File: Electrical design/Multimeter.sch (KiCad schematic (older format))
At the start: 36 parts, among them P101 CONN_02X07, P102 CONN_01X06, Q101 Q_PMOS_GSD, Q102 Q_NMOS_GSD, U101 STM32F373R8Tx, U102 ILI9341_LCD_Breakout, U103 BD4835, Y101 8 MHz

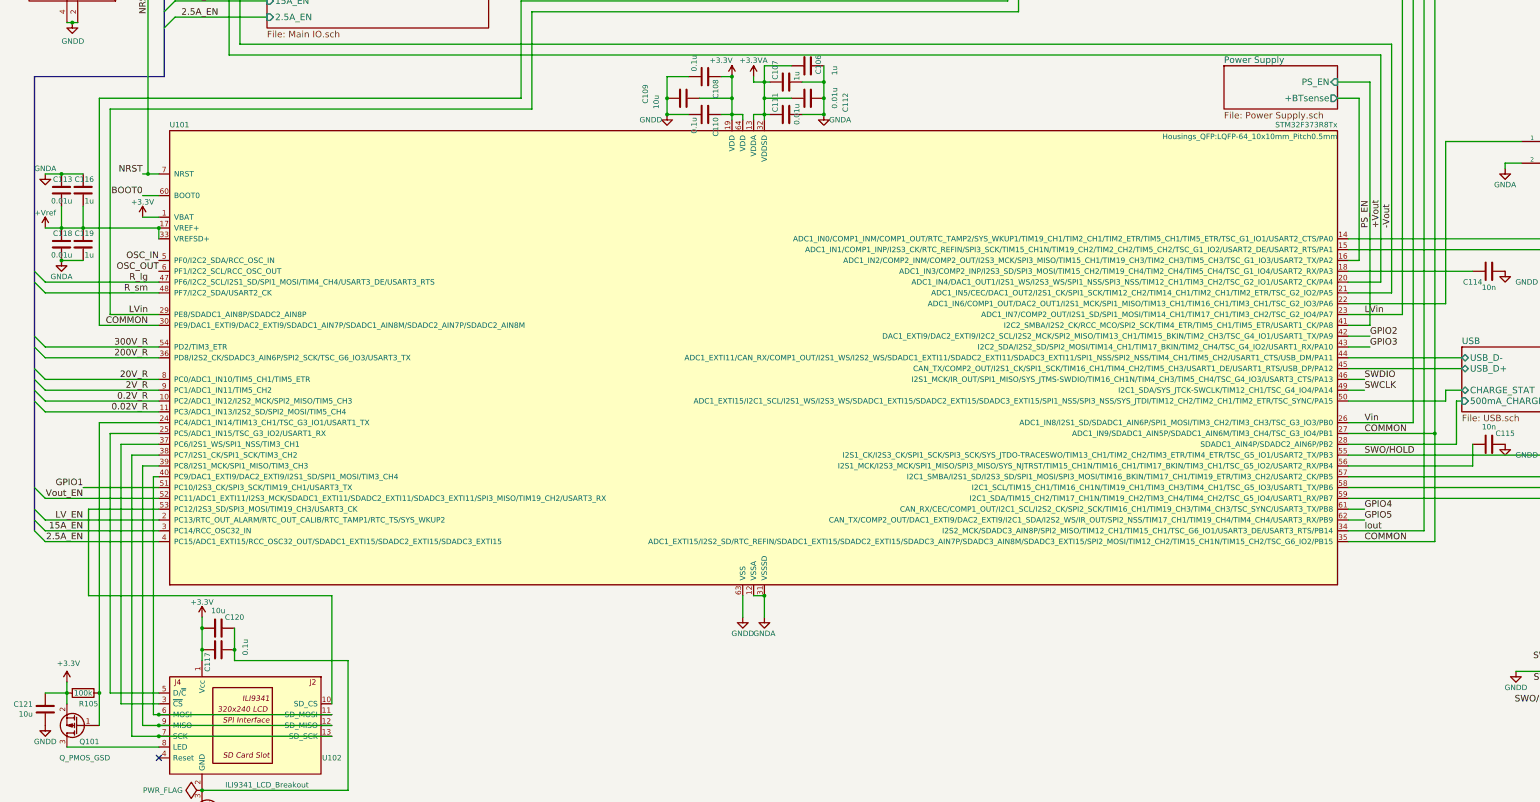
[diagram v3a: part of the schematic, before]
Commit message: Added PCB layout.
Also minor changes to schematic, the most major being changes
to which MCU pins control what to make the PCB layout easier.
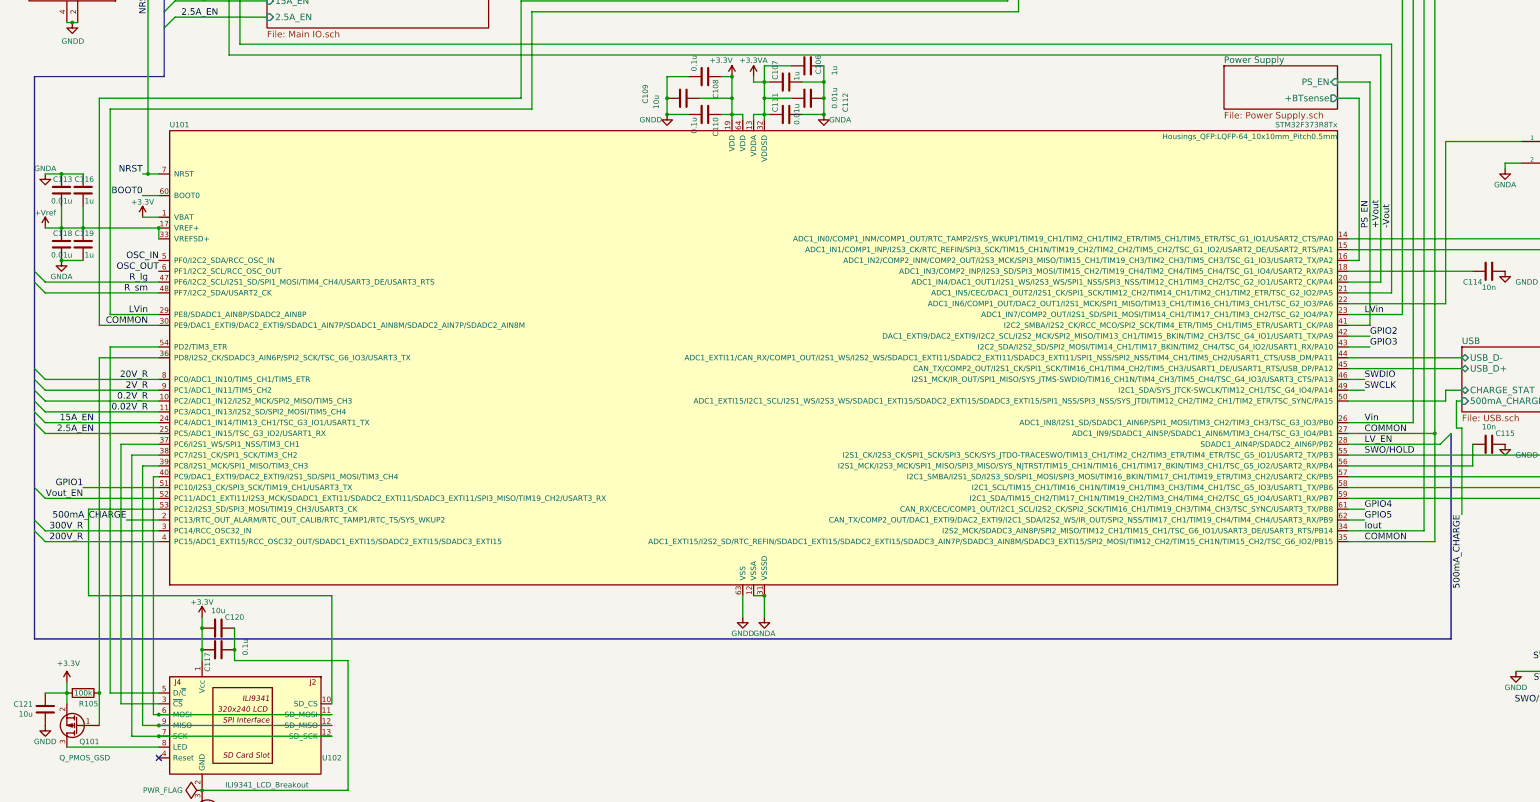
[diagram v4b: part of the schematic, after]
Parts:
- JP101: footprint Pin_Headers:Pin_Header_Straight_1x02 -> my footprints:Pin_Header_Straight_1x02
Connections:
- net USB/500mA_CHARGE is gone; now on net LV_EN: U101.28 (SDADC1_AIN4P/SDADC2_AIN6P/PB2)
- net 15A_EN: now also U101.24 (PC4/ADC1_IN14/TIM13_CH1/TSC_G3_IO1/USART1_TX); no longer U101.3 (PC14/RCC_OSC32_IN)
- net 2.5A_EN: now also U101.25 (PC5/ADC1_IN15/TSC_G3_IO2/USART1_RX); no longer U101.4 (PC15/ADC1_EXTI15/RCC_OSC32_OUT/SDADC1_EXTI15/SDADC2_EXTI15/SDADC3_EXTI15)
- net 200V_R: now also U101.4 (PC15/ADC1_EXTI15/RCC_OSC32_OUT/SDADC1_EXTI15/SDADC2_EXTI15/SDADC3_EXTI15); no longer U101.36 (PD8/I2S2_CK/SDADC3_AIN6P/SPI2_SCK/TSC_G6_IO3/USART3_TX)
- net 300V_R: now also U101.3 (PC14/RCC_OSC32_IN); no longer U101.54 (PD2/TIM3_ETR)
- net LV_EN: no longer U101.2 (PC13/RTC_OUT_ALARM/RTC_OUT_CALIB/RTC_TAMP1/RTC_TS/SYS_WKUP2)
- net at Q101.1 (G), R105.1: now also U101.36 (PD8/I2S2_CK/SDADC3_AIN6P/SPI2_SCK/TSC_G6_IO3/USART3_TX); no longer U101.24 (PC4/ADC1_IN14/TIM13_CH1/TSC_G3_IO1/USART1_TX)
- net at U102.5 (D/~C): now also U101.54 (PD2/TIM3_ETR); no longer U101.25 (PC5/ADC1_IN15/TSC_G3_IO2/USART1_RX)
- new net 500mA_CHARGE: U101.2 (PC13/RTC_OUT_ALARM/RTC_OUT_CALIB/RTC_TAMP1/RTC_TS/SYS_WKUP2)
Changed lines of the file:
@@
 Sheet 1 5
 Title "Multimeter – Overview"
-Date "2016-06-22"
-Rev "0.5"
+Date "2016-07-02"
+Rev "0.6"
 Comp ""
-Comment1 ""
+Comment1 "Licensed under the GNU GPL v3"
 Comment2 ""
 Comment3 ""
@@
 F 0 "JP101" V 1450 1898 50  0000 L CNN
 F 1 "BOOT0" H 1460 1790 50  0001 C CNN
-F 2 "Pin_Headers:Pin_Header_Straight_1x02" H 1450 1850 50  0001 C CNN
+F 2 "my footprints:Pin_Header_Straight_1x02" H 1450 1850 50  0001 C CNN
 F 3 "" H 1450 1850 50  0000 C CNN
 	1    1450 1850
@@
 	700  5900 800  6000
 Entry Wire Line
-	700  6400 800  6500
-Entry Wire Line
-	700  6500 800  6600
+	700  7100 800  7200
+Entry Wire Line
+	700  7200 800  7300
 Entry Wire Line
 	700  6700 800  6800
@@
 	700  7800 800  7900
 Entry Wire Line
-	700  8000 800  8100
-Entry Wire Line
 	700  8100 800  8200
-Text Label 1150 8300 2    60   ~ 0
+Text Label 1250 7300 2    60   ~ 0
 2.5A_EN
-Text Label 1150 8200 2    60   ~ 0
+Text Label 1250 7200 2    60   ~ 0
 15A_EN
-Text Label 1150 8100 2    60   ~ 0
+Text Label 13000 7400 0    60   ~ 0
 LV_EN
 Text Label 1750 5900 2    60   ~ 0
@@
 Entry Wire Line
 	700  7000 800  7100
-Text Label 1750 6500 2    60   ~ 0
+Text Label 1150 8200 2    60   ~ 0
 300V_R
-Text Label 1750 6600 2    60   ~ 0
+Text Label 1150 8300 2    60   ~ 0
 200V_R
 Text Label 1750 6800 2    60   ~ 0
@@
 PS_EN
 $Comp
-L +3.3V #PWR019
+L +3.3V #PWR018
 U 1 1 574F1A1A
 P 1000 9600
-F 0 "#PWR019" H 1000 9450 50  0001 C CNN
+F 0 "#PWR018" H 1000 9450 50  0001 C CNN
 F 1 "+3.3V" H 1015 9773 50  0000 C CNN
 F 2 "" H 1000 9600 50  0000 C CNN
@@
 $EndComp
 $Comp
-L GNDD #PWR020
+L GNDD #PWR019
 U 1 1 574F2BEE
 P 800 10000
-F 0 "#PWR020" H 800 9750 50  0001 C CNN
+F 0 "#PWR019" H 800 9750 50  0001 C CNN
 F 1 "GNDD" H 800 9850 50  0000 C CNN
 F 2 "" H 800 10000 50  0000 C CNN
@@
 $EndComp
 $Comp
-L GNDD #PWR021
+L GNDD #PWR020
 U 1 1 575818F5
 P 14300 7400
-F 0 "#PWR021" H 14300 7150 50  0001 C CNN
+F 0 "#PWR020" H 14300 7150 50  0001 C CNN
 F 1 "GNDD" H 14500 7300 50  0000 C CNN
 F 2 "" H 14300 7400 50  0000 C CNN
@@
 GPIO5
 $Comp
-L +3.3V #PWR022
+L +3.3V #PWR021
 U 1 1 5758136C
 P 7100 2300
-F 0 "#PWR022" H 7100 2150 50  0001 C CNN
+F 0 "#PWR021" H 7100 2150 50  0001 C CNN
 F 1 "+3.3V" H 7115 2473 50  0000 C CNN
 F 2 "" H 7100 2300 50  0000 C CNN
@@
 $EndComp
 $Comp
-L +3.3VA #PWR023
+L +3.3VA #PWR022
 U 1 1 5758157D
 P 6200 2300
-F 0 "#PWR023" H 6200 2150 50  0001 C CNN
+F 0 "#PWR022" H 6200 2150 50  0001 C CNN
 F 1 "+3.3VA" H 6215 2473 50  0000 C CNN
 F 2 "" H 6200 2300 50  0000 C CNN
@@
 $EndComp
 $Comp
-L +Vref #PWR024
+L +Vref #PWR023
 U 1 1 57581671
 P 6000 2400
-F 0 "#PWR024" H 6000 2250 50  0001 C CNN
+F 0 "#PWR023" H 6000 2250 50  0001 C CNN
 F 1 "+Vref" H 6015 2573 50  0000 C CNN
 F 2 "" H 6000 2400 50  0000 C CNN
@@
 $EndComp
 $Comp
-L GNDA #PWR025
+L GNDA #PWR024
 U 1 1 57581765
 P 6200 2900
-F 0 "#PWR025" H 6200 2650 50  0001 C CNN
+F 0 "#PWR024" H 6200 2650 50  0001 C CNN
 F 1 "GNDA" H 6205 2727 50  0000 C CNN
 F 2 "" H 6200 2900 50  0000 C CNN
@@
 $EndComp
 $Comp
-L GNDD #PWR026
+L GNDD #PWR025
 U 1 1 57581859
 P 7100 2900
-F 0 "#PWR026" H 7100 2650 50  0001 C CNN
+F 0 "#PWR025" H 7100 2650 50  0001 C CNN
 F 1 "GNDD" H 7105 2727 50  0000 C CNN
 F 2 "" H 7100 2900 50  0000 C CNN
@@
 $EndComp
 $Comp
-L GNDA #PWR027
+L GNDA #PWR026
 U 1 1 575E7712
 P 14300 4850
-F 0 "#PWR027" H 14300 4600 50  0001 C CNN
+F 0 "#PWR026" H 14300 4600 50  0001 C CNN
 F 1 "GNDA" H 14300 4700 50  0000 C CNN
 F 2 "" H 14300 4850 50  0000 C CNN
@@
 $EndComp
 $Comp
-L +3.3V #PWR028
+L +3.3V #PWR027
 U 1 1 576110F8
 P 1050 2600
-F 0 "#PWR028" H 1050 2450 50  0001 C CNN
+F 0 "#PWR027" H 1050 2450 50  0001 C CNN
 F 1 "+3.3V" H 1065 2773 50  0000 C CNN
 F 2 "" H 1050 2600 50  0000 C CNN
@@
 $EndComp
 $Comp
-L GNDD #PWR029
+L GNDD #PWR028
 U 1 1 5761132F
 P 1050 3500
-F 0 "#PWR029" H 1050 3250 50  0001 C CNN
+F 0 "#PWR028" H 1050 3250 50  0001 C CNN
 F 1 "GNDD" H 1055 3327 50  0000 C CNN
 F 2 "" H 1050 3500 50  0000 C CNN
@@
 $EndComp
 $Comp
-L GNDA #PWR030
+L GNDA #PWR029
 U 1 1 57634337
 P 800 4900
-F 0 "#PWR030" H 800 4650 50  0001 C CNN
+F 0 "#PWR029" H 800 4650 50  0001 C CNN
 F 1 "GNDA" H 800 4950 50  0000 C CNN
 F 2 "" H 800 4900 50  0000 C CNN
@@
 $EndComp
 $Comp
-L PWR_FLAG #FLG031
+L PWR_FLAG #FLG030
 U 1 1 5767D4A4
 P 2250 10600
-F 0 "#FLG031" H 2250 10695 50  0001 C CNN
+F 0 "#FLG030" H 2250 10695 50  0001 C CNN
 F 1 "PWR_FLAG" V 2250 10778 50  0000 L CNN
 F 2 "" H 2250 10600 50  0000 C CNN
@@
 	13750 7000 13750 6900
 Wire Wire Line
-	12850 7400 13850 7400
-Wire Wire Line
-	13850 7400 13850 7000
-Wire Wire Line
 	13000 6900 12850 6900
 Wire Wire Line
@@
 Connection ~ 2250 9100
 Wire Bus Line
-	700  4000 700  8200
+	700  4000 700  9200
 Wire Wire Line
 	800  5900 1850 5900
@@
 	1850 8200 800  8200
 Wire Wire Line
-	800  8100 1850 8100
-Wire Wire Line
 	1850 7000 800  7000
 Wire Wire Line
@@
 	1850 6800 800  6800
 Wire Wire Line
-	800  6600 1850 6600
-Wire Wire Line
-	1850 6500 800  6500
+	800  7300 1850 7300
+Wire Wire Line
+	1850 7200 800  7200
 Wire Wire Line
 	1850 7500 1600 7500
@@
 	1500 9800 1850 9800
 Wire Wire Line
-	1850 7300 1400 7300
-Wire Wire Line
-	1400 7300 1400 9700
+	1400 6500 1400 9700
 Wire Wire Line
 	1400 9700 1850 9700
 Wire Wire Line
-	1850 7200 1300 7200
-Wire Wire Line
 	1850 7100 800  7100
 Wire Wire Line
 	1000 10200 1850 10200
-Wire Wire Line
-	1300 7200 1300 10000
 Wire Wire Line
 	1000 9600 1000 9800
@@
 Wire Wire Line
 	3600 10600 2250 10600
+Wire Wire Line
+	1300 6600 1850 6600
+Wire Wire Line
+	1400 6500 1850 6500
+Wire Wire Line
+	1300 6600 1300 10000
+Text Label 13900 8050 3    60   ~ 0
+500mA_CHARGE
+Text Label 1550 8100 2    60   ~ 0
+500mA_CHARGE
+Wire Wire Line
+	1550 8100 1850 8100
+Wire Bus Line
+	700  9200 13800 9200
+Wire Bus Line
+	13800 9200 13800 7300
+Entry Wire Line
+	13700 7400 13800 7300
+Wire Wire Line
+	12850 7400 13700 7400
+Wire Wire Line
+	13850 7000 13850 7250
+Wire Wire Line
+	13850 7250 13900 7250
+Wire Wire Line
+	13900 7250 13900 8050
 $EndSCHEMATC

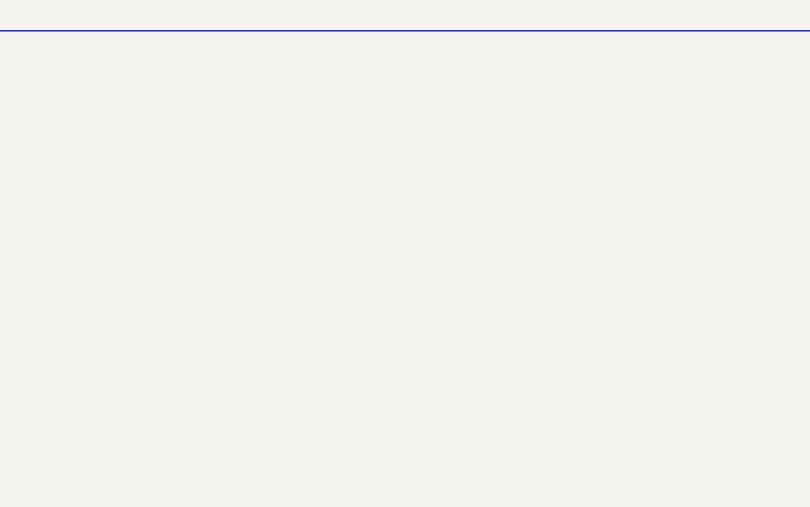
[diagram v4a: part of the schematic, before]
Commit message: Tied ground nets together, fixed clearance issues, added copper pours / zones.
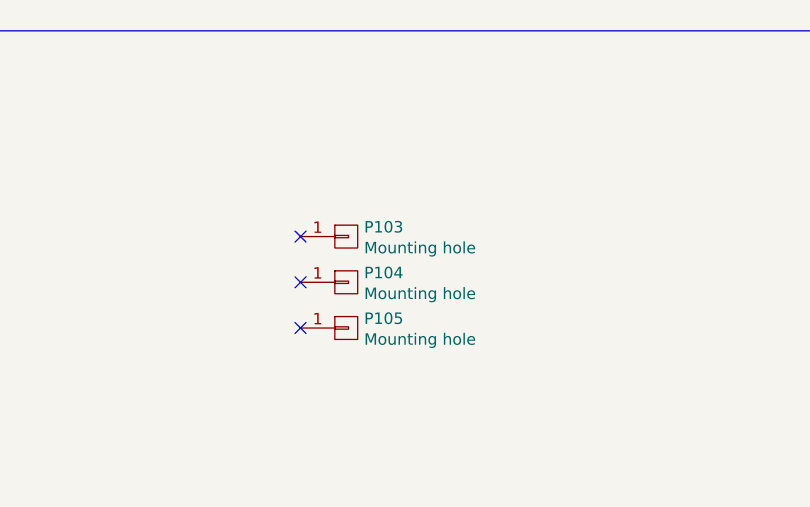
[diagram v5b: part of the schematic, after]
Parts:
- added P103, P104, P105: Mounting hole, Mounting_Holes:MountingHole_3.2mm_M3, symbol CONN_01X01
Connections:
- no-connect marks 1 -> 4
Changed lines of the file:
@@
 Sheet 1 5
 Title "Multimeter – Overview"
-Date "2016-07-02"
-Rev "0.6"
+Date "2016-07-04"
+Rev "0.7"
 Comp ""
 Comment1 "Licensed under the GNU GPL v3"
@@
 $EndSheet
 $Comp
-L +3.3V #PWR01
+L +3.3V #PWR111
 U 1 1 5739D7E6
 P 7150 4000
-F 0 "#PWR01" H 7150 3850 50  0001 C CNN
+F 0 "#PWR111" H 7150 3850 50  0001 C CNN
 F 1 "+3.3V" H 7050 4150 50  0000 C CNN
 F 2 "" H 7150 4000 50  0000 C CNN
@@
 $EndComp
 $Comp
-L +3.3VA #PWR02
+L +3.3VA #PWR112
 U 1 1 5739D86E
 P 7350 4000
-F 0 "#PWR02" H 7350 3850 50  0001 C CNN
+F 0 "#PWR112" H 7350 3850 50  0001 C CNN
 F 1 "+3.3VA" H 7350 4150 50  0000 C CNN
 F 2 "" H 7350 4000 50  0000 C CNN
@@
 $EndComp
 $Comp
-L GNDA #PWR03
+L GNDA #PWR124
 U 1 1 5739DB72
 P 7450 9000
-F 0 "#PWR03" H 7450 8750 50  0001 C CNN
+F 0 "#PWR124" H 7450 8750 50  0001 C CNN
 F 1 "GNDA" H 7450 8850 50  0000 C CNN
 F 2 "" H 7450 9000 50  0000 C CNN
@@
 $EndComp
 $Comp
-L +Vref #PWR04
+L +Vref #PWR118
 U 1 1 5739DCE2
 P 800 5400
-F 0 "#PWR04" H 800 5250 50  0001 C CNN
+F 0 "#PWR118" H 800 5250 50  0001 C CNN
 F 1 "+Vref" H 800 5540 50  0000 C CNN
 F 2 "" H 800 5400 50  0000 C CNN
@@
 $EndComp
 $Comp
-L +3.3V #PWR05
+L +3.3V #PWR117
 U 1 1 5739DD6A
 P 1700 5300
-F 0 "#PWR05" H 1700 5150 50  0001 C CNN
+F 0 "#PWR117" H 1700 5150 50  0001 C CNN
 F 1 "+3.3V" H 1700 5440 50  0000 C CNN
 F 2 "" H 1700 5300 50  0000 C CNN
@@
 $EndComp
 $Comp
-L GNDD #PWR06
+L GNDD #PWR123
 U 1 1 573A7ED7
 P 7250 9000
-F 0 "#PWR06" H 7250 8750 50  0001 C CNN
+F 0 "#PWR123" H 7250 8750 50  0001 C CNN
 F 1 "GNDD" H 7250 8850 50  0000 C CNN
 F 2 "" H 7250 9000 50  0000 C CNN
@@
 $EndComp
 $Comp
-L GNDD #PWR07
+L GNDD #PWR113
 U 1 1 573D4987
 P 6550 4350
-F 0 "#PWR07" H 6550 4100 50  0001 C CNN
+F 0 "#PWR113" H 6550 4100 50  0001 C CNN
 F 1 "GNDD" H 6400 4300 50  0000 C CNN
 F 2 "" H 6550 4350 50  0000 C CNN
@@
 $EndComp
 $Comp
-L GNDA #PWR08
+L GNDA #PWR114
 U 1 1 573D4A23
 P 8000 4350
-F 0 "#PWR08" H 8000 4100 50  0001 C CNN
+F 0 "#PWR114" H 8000 4100 50  0001 C CNN
 F 1 "GNDA" H 8150 4300 50  0000 C CNN
 F 2 "" H 8000 4350 50  0000 C CNN
@@
 $EndComp
 $Comp
-L GNDA #PWR09
+L GNDA #PWR119
 U 1 1 57427F89
 P 950 5700
-F 0 "#PWR09" H 950 5450 50  0001 C CNN
+F 0 "#PWR119" H 950 5450 50  0001 C CNN
 F 1 "GNDA" H 950 5550 50  0000 C CNN
 F 2 "" H 950 5700 50  0000 C CNN
@@
 SWDIO
 $Comp
-L GNDD #PWR010
+L GNDD #PWR126
 U 1 1 57494687
 P 14400 9500
-F 0 "#PWR010" H 14400 9250 50  0001 C CNN
+F 0 "#PWR126" H 14400 9250 50  0001 C CNN
 F 1 "GNDD" H 14400 9350 50  0000 C CNN
 F 2 "" H 14400 9500 50  0000 C CNN
@@
 SWCLK
 $Comp
-L +3.3V #PWR011
+L +3.3V #PWR125
 U 1 1 574949A0
 P 15050 9300
-F 0 "#PWR011" H 15050 9150 50  0001 C CNN
+F 0 "#PWR125" H 15050 9150 50  0001 C CNN
 F 1 "+3.3V" H 15050 9440 50  0000 C CNN
 F 2 "" H 15050 9300 50  0000 C CNN
@@
 $EndComp
 $Comp
-L GNDD #PWR012
+L GNDD #PWR120
 U 1 1 5749D81E
 P 14300 5800
-F 0 "#PWR012" H 14300 5550 50  0001 C CNN
+F 0 "#PWR120" H 14300 5550 50  0001 C CNN
 F 1 "GNDD" H 14500 5700 50  0000 C CNN
 F 2 "" H 14300 5800 50  0000 C CNN
@@
 $EndComp
 $Comp
-L GNDD #PWR013
+L GNDD #PWR101
 U 1 1 574B72E4
 P 650 1200
-F 0 "#PWR013" H 650 950 50  0001 C CNN
+F 0 "#PWR101" H 650 950 50  0001 C CNN
 F 1 "GNDD" H 655 1027 50  0000 C CNN
 F 2 "" H 650 1200 50  0000 C CNN
@@
 $EndComp
 $Comp
-L +3.3V #PWR014
+L +3.3V #PWR102
 U 1 1 574BD1A9
 P 1450 1750
-F 0 "#PWR014" H 1450 1600 50  0001 C CNN
+F 0 "#PWR102" H 1450 1600 50  0001 C CNN
 F 1 "+3.3V" H 1465 1923 50  0000 C CNN
 F 2 "" H 1450 1750 50  0000 C CNN
@@
 $EndComp
 $Comp
-L GNDD #PWR015
+L GNDD #PWR105
 U 1 1 574BD2BB
 P 1450 2350
-F 0 "#PWR015" H 1450 2100 50  0001 C CNN
+F 0 "#PWR105" H 1450 2100 50  0001 C CNN
 F 1 "GNDD" H 1455 2177 50  0000 C CNN
 F 2 "" H 1450 2350 50  0000 C CNN
@@
 $EndComp
 $Comp
-L GNDD #PWR016
+L GNDD #PWR129
 U 1 1 574DD0AD
 P 2250 11000
-F 0 "#PWR016" H 2250 10750 50  0001 C CNN
+F 0 "#PWR129" H 2250 10750 50  0001 C CNN
 F 1 "GNDD" H 2250 10850 50  0000 C CNN
 F 2 "" H 2250 11000 50  0000 C CNN
@@
 $EndComp
 $Comp
-L +3.3V #PWR017
+L +3.3V #PWR122
 U 1 1 574DD24C
 P 2250 9000
-F 0 "#PWR017" H 2250 8850 50  0001 C CNN
+F 0 "#PWR122" H 2250 8850 50  0001 C CNN
 F 1 "+3.3V" H 2250 9140 50  0000 C CNN
 F 2 "" H 2250 9000 50  0000 C CNN
@@
 PS_EN
 $Comp
-L +3.3V #PWR018
+L +3.3V #PWR127
 U 1 1 574F1A1A
 P 1000 9600
-F 0 "#PWR018" H 1000 9450 50  0001 C CNN
+F 0 "#PWR127" H 1000 9450 50  0001 C CNN
 F 1 "+3.3V" H 1015 9773 50  0000 C CNN
 F 2 "" H 1000 9600 50  0000 C CNN
@@
 $EndComp
 $Comp
-L GNDD #PWR019
+L GNDD #PWR128
 U 1 1 574F2BEE
 P 800 10000
-F 0 "#PWR019" H 800 9750 50  0001 C CNN
+F 0 "#PWR128" H 800 9750 50  0001 C CNN
 F 1 "GNDD" H 800 9850 50  0000 C CNN
 F 2 "" H 800 10000 50  0000 C CNN
@@
 $EndComp
 $Comp
-L GNDD #PWR020
+L GNDD #PWR121
 U 1 1 575818F5
 P 14300 7400
-F 0 "#PWR020" H 14300 7150 50  0001 C CNN
+F 0 "#PWR121" H 14300 7150 50  0001 C CNN
 F 1 "GNDD" H 14500 7300 50  0000 C CNN
 F 2 "" H 14300 7400 50  0000 C CNN
@@
 GPIO5
 $Comp
-L +3.3V #PWR021
+L +3.3V #PWR104
 U 1 1 5758136C
 P 7100 2300
-F 0 "#PWR021" H 7100 2150 50  0001 C CNN
+F 0 "#PWR104" H 7100 2150 50  0001 C CNN
 F 1 "+3.3V" H 7115 2473 50  0000 C CNN
 F 2 "" H 7100 2300 50  0000 C CNN
@@
 $EndComp
 $Comp
-L +3.3VA #PWR022
+L +3.3VA #PWR103
 U 1 1 5758157D
 P 6200 2300
-F 0 "#PWR022" H 6200 2150 50  0001 C CNN
+F 0 "#PWR103" H 6200 2150 50  0001 C CNN
 F 1 "+3.3VA" H 6215 2473 50  0000 C CNN
 F 2 "" H 6200 2300 50  0000 C CNN
@@
 $EndComp
 $Comp
-L +Vref #PWR023
+L +Vref #PWR106
 U 1 1 57581671
 P 6000 2400
-F 0 "#PWR023" H 6000 2250 50  0001 C CNN
+F 0 "#PWR106" H 6000 2250 50  0001 C CNN
 F 1 "+Vref" H 6015 2573 50  0000 C CNN
 F 2 "" H 6000 2400 50  0000 C CNN
@@
 $EndComp
 $Comp
-L GNDA #PWR024
+L GNDA #PWR108
 U 1 1 57581765
 P 6200 2900
-F 0 "#PWR024" H 6200 2650 50  0001 C CNN
+F 0 "#PWR108" H 6200 2650 50  0001 C CNN
 F 1 "GNDA" H 6205 2727 50  0000 C CNN
 F 2 "" H 6200 2900 50  0000 C CNN
@@
 $EndComp
 $Comp
-L GNDD #PWR025
+L GNDD #PWR109
 U 1 1 57581859
 P 7100 2900
-F 0 "#PWR025" H 7100 2650 50  0001 C CNN
+F 0 "#PWR109" H 7100 2650 50  0001 C CNN
 F 1 "GNDD" H 7105 2727 50  0000 C CNN
 F 2 "" H 7100 2900 50  0000 C CNN
@@
 $EndComp
 $Comp
-L GNDA #PWR026
+L GNDA #PWR115
 U 1 1 575E7712
 P 14300 4850
-F 0 "#PWR026" H 14300 4600 50  0001 C CNN
+F 0 "#PWR115" H 14300 4600 50  0001 C CNN
 F 1 "GNDA" H 14300 4700 50  0000 C CNN
 F 2 "" H 14300 4850 50  0000 C CNN
@@
 $EndComp
 $Comp
-L +3.3V #PWR027
+L +3.3V #PWR107
 U 1 1 576110F8
 P 1050 2600
-F 0 "#PWR027" H 1050 2450 50  0001 C CNN
+F 0 "#PWR107" H 1050 2450 50  0001 C CNN
 F 1 "+3.3V" H 1065 2773 50  0000 C CNN
 F 2 "" H 1050 2600 50  0000 C CNN
@@
 $EndComp
 $Comp
-L GNDD #PWR028
+L GNDD #PWR110
 U 1 1 5761132F
 P 1050 3500
-F 0 "#PWR028" H 1050 3250 50  0001 C CNN
+F 0 "#PWR110" H 1050 3250 50  0001 C CNN
 F 1 "GNDD" H 1055 3327 50  0000 C CNN
 F 2 "" H 1050 3500 50  0000 C CNN
@@
 $EndComp
 $Comp
-L GNDA #PWR029
+L GNDA #PWR116
 U 1 1 57634337
 P 800 4900
-F 0 "#PWR029" H 800 4650 50  0001 C CNN
+F 0 "#PWR116" H 800 4650 50  0001 C CNN
 F 1 "GNDA" H 800 4950 50  0000 C CNN
 F 2 "" H 800 4900 50  0000 C CNN
@@
 $EndComp
 $Comp
-L PWR_FLAG #FLG030
+L PWR_FLAG #FLG101
 U 1 1 5767D4A4
 P 2250 10600
-F 0 "#FLG030" H 2250 10695 50  0001 C CNN
+F 0 "#FLG101" H 2250 10695 50  0001 C CNN
 F 1 "PWR_FLAG" V 2250 10778 50  0000 L CNN
 F 2 "" H 2250 10600 50  0000 C CNN
@@
 Wire Wire Line
 	13900 7250 13900 8050
+$Comp
+L CONN_01X01 P103
+U 1 1 57779E1F
+P 9700 10100
+F 0 "P103" H 9778 10141 50  0000 L CNN
+F 1 "Mounting hole" H 9778 10050 50  0000 L CNN
+F 2 "Mounting_Holes:MountingHole_3.2mm_M3" H 9700 10100 50  0001 C CNN
+F 3 "" H 9700 10100 50  0000 C CNN
+	1    9700 10100
+	1    0    0    -1
+$EndComp
+$Comp
+L CONN_01X01 P104
+U 1 1 57779F8D
+P 9700 10300
+F 0 "P104" H 9778 10341 50  0000 L CNN
+F 1 "Mounting hole" H 9778 10250 50  0000 L CNN
+F 2 "Mounting_Holes:MountingHole_3.2mm_M3" H 9700 10300 50  0001 C CNN
+F 3 "" H 9700 10300 50  0000 C CNN
+	1    9700 10300
+	1    0    0    -1
+$EndComp
+$Comp
+L CONN_01X01 P105
+U 1 1 5777A0A6
+P 9700 10500
+F 0 "P105" H 9778 10541 50  0000 L CNN
+F 1 "Mounting hole" H 9778 10450 50  0000 L CNN
+F 2 "Mounting_Holes:MountingHole_3.2mm_M3" H 9700 10500 50  0001 C CNN
+F 3 "" H 9700 10500 50  0000 C CNN
+	1    9700 10500
+	1    0    0    -1
+$EndComp
+NoConn ~ 9500 10100
+NoConn ~ 9500 10300
+NoConn ~ 9500 10500
 $EndSCHEMATC
